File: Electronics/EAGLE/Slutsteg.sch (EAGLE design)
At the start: 151 parts, among them CN1 OSTYK33102030-2, CN2 OSTYK33102030-2, CN3 OSTYK33102030-2, CN4 OSTYK33102030-2, IC1 SPX1117M3-L-3-3_TR, IC10 LM324D, IC11 L78M12ABDT-TR, IC3 ESP32-WROVER-IE-4MB, IC4 TM8211, IC5 LM358LVIDR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

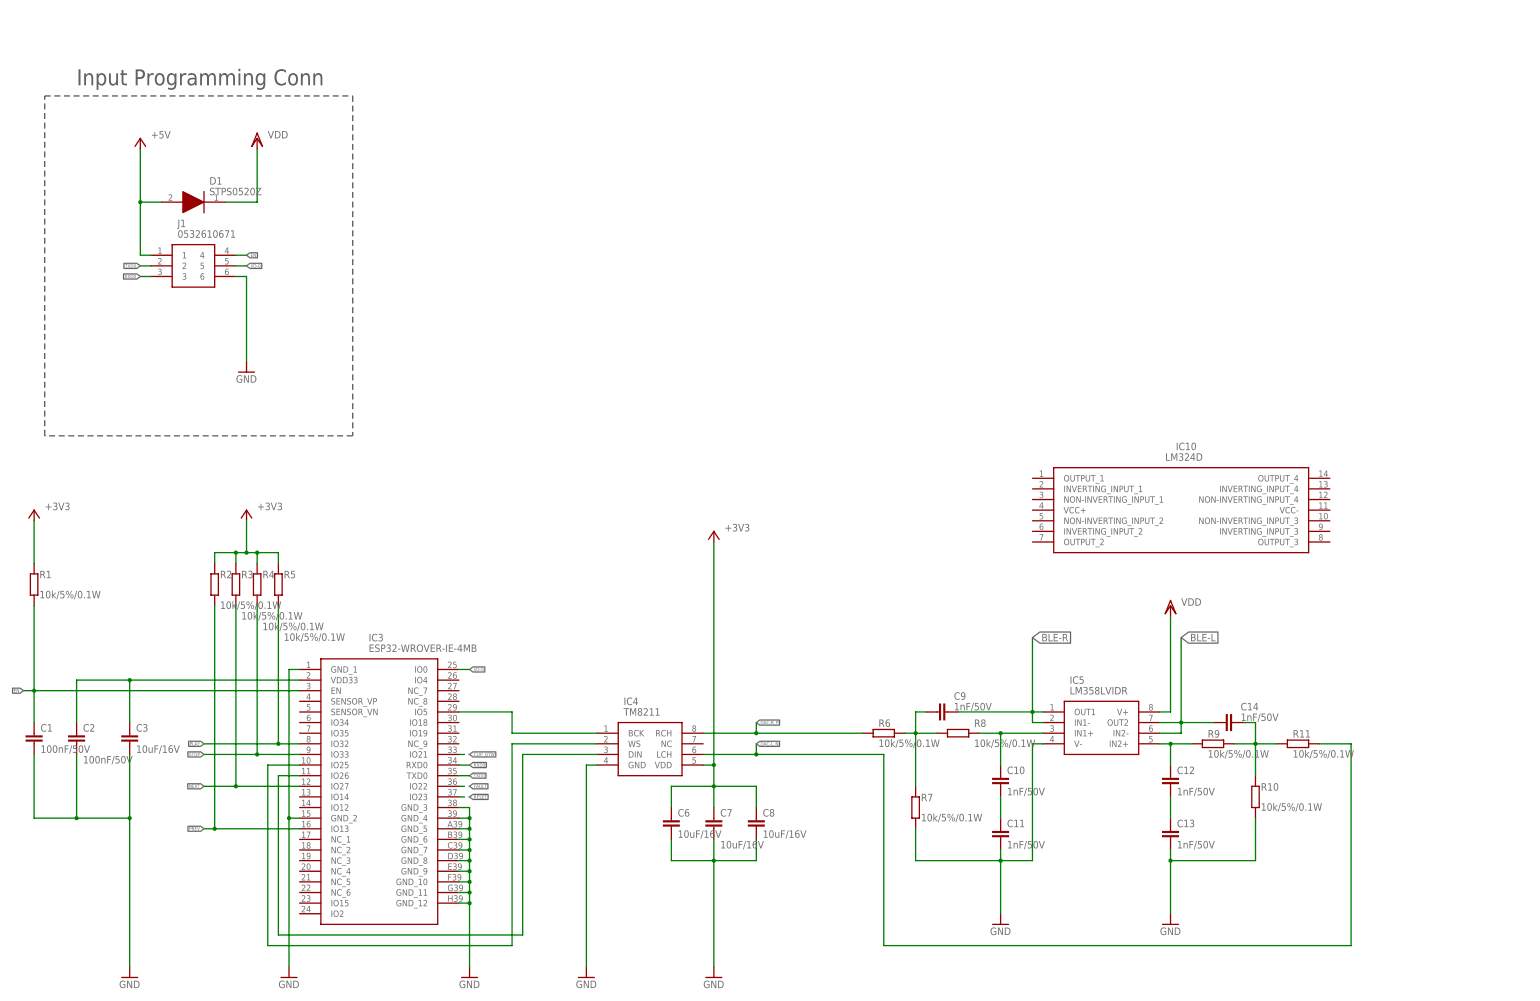
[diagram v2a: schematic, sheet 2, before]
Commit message: Changed OP-AMP for the DAC
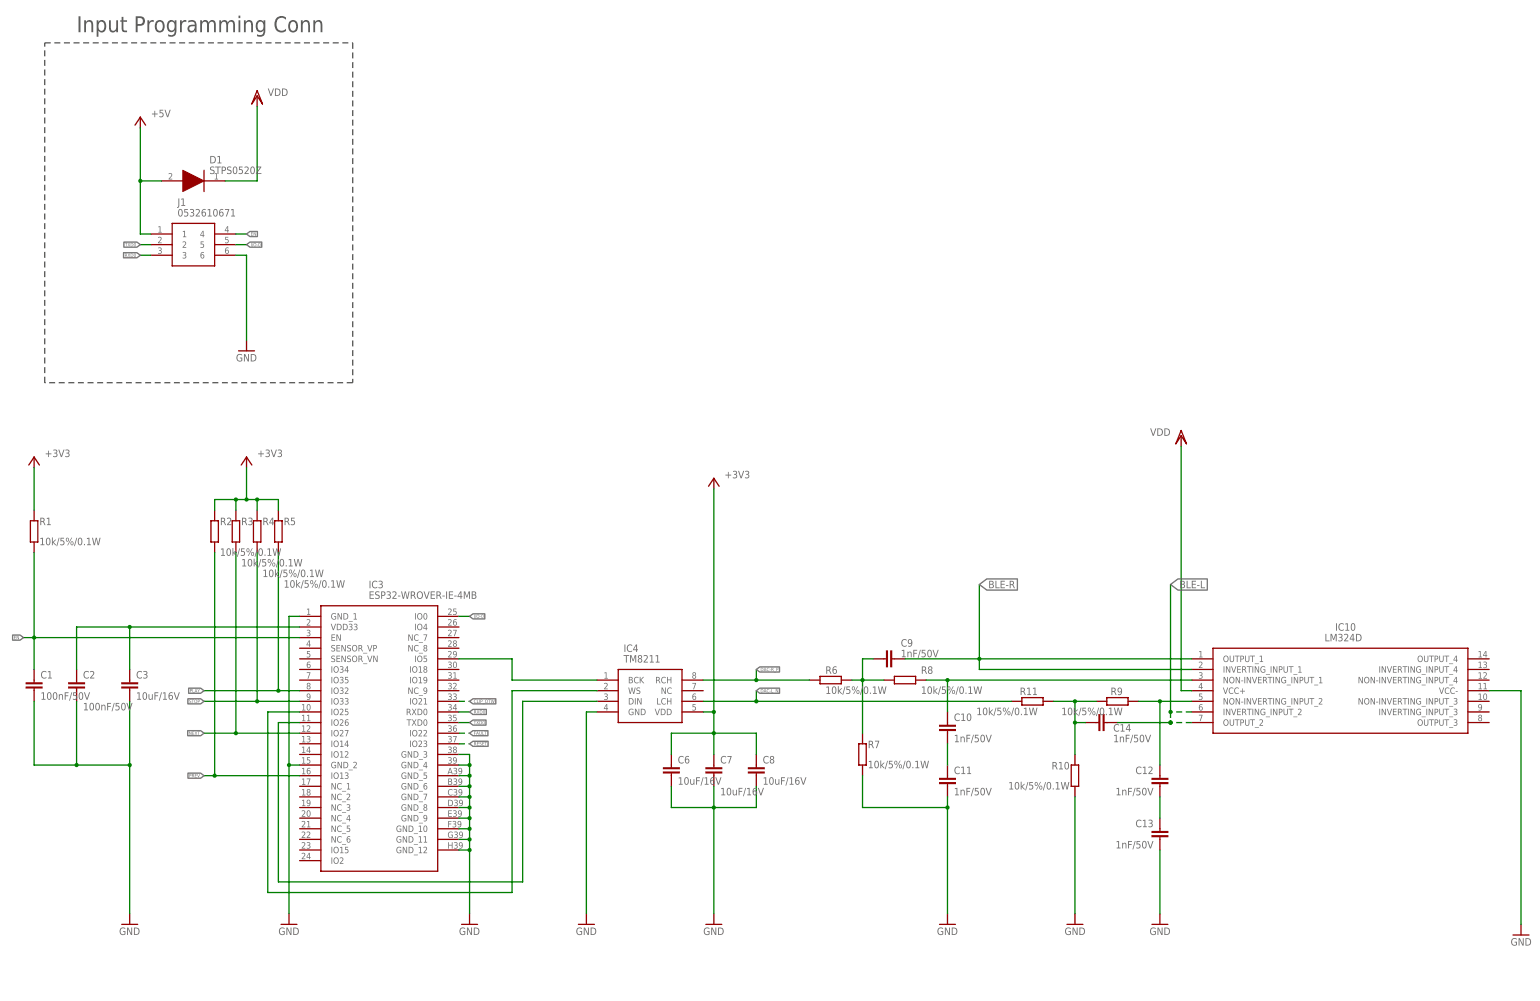
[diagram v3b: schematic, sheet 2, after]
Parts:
- removed IC5: LM358LVIDR, SamacSys_Parts:LM358LVIDR
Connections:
- net BLE-L: now also IC10.INVERTING_INPUT_2, IC10.OUTPUT_2; no longer IC5.IN2-, IC5.OUT2
- net BLE-R: now also IC10.INVERTING_INPUT_1, IC10.OUTPUT_1; no longer IC5.IN1-, IC5.OUT1
- net GND: now also IC10.VCC-; no longer IC5.V-
- net N$79: now also IC10.NON-INVERTING_INPUT_1; no longer IC5.IN1+
- net N$81: now also IC10.NON-INVERTING_INPUT_2; no longer IC5.IN2+
- net VDD: now also IC10.VCC+; no longer IC5.V+
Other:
- moved on the sheet: C1, C10, C11, C12, C13, C14, C2, C3, C5, C6, C7, C8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

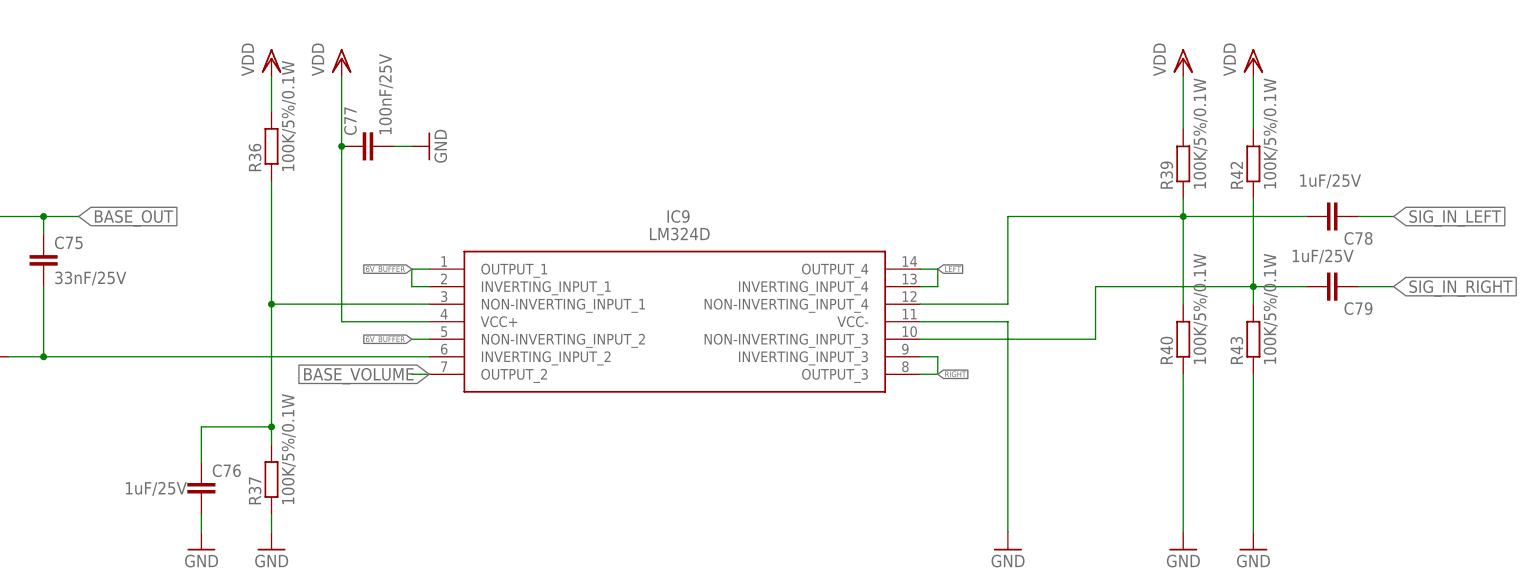
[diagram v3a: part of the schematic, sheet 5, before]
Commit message: Changed footprints for caps
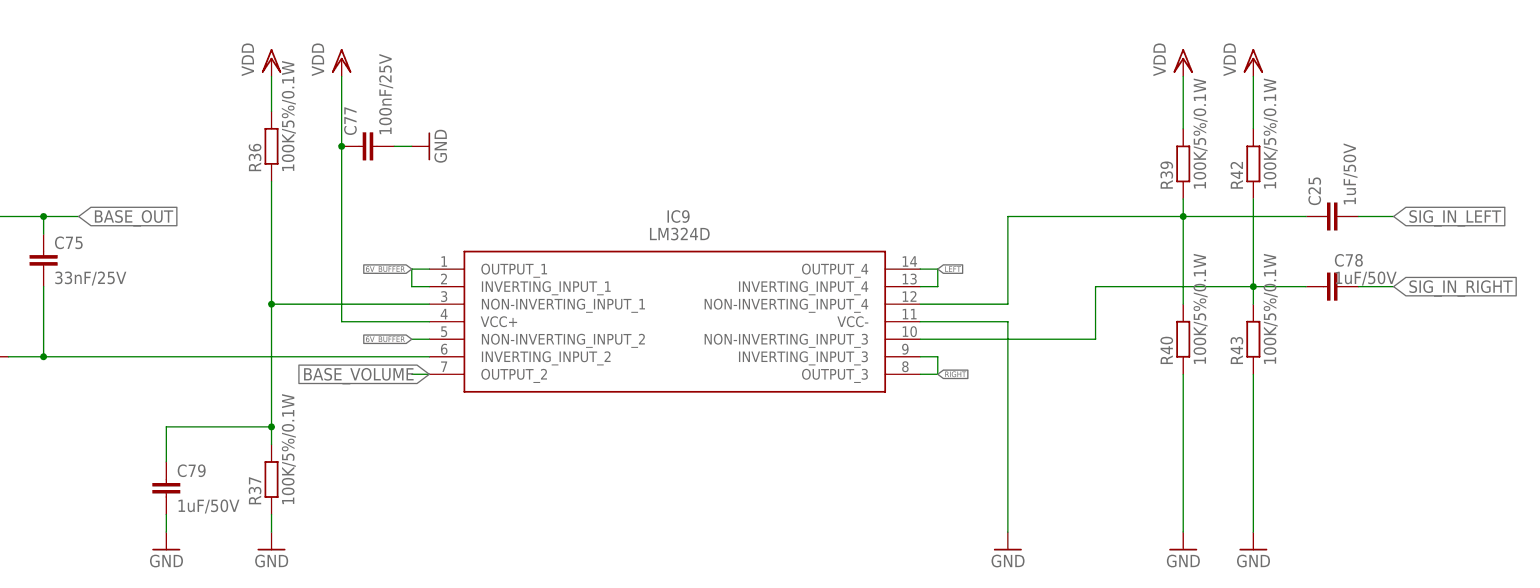
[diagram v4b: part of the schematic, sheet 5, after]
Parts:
- removed C76: 1uF/25V, rcl:C-EUC0603
- added C25: 1uF/50V, rcl:C-EUC0805
- C78, C79: value 1uF/25V -> 1uF/50V; device rcl:C-EUC0603 -> rcl:C-EUC0805
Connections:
- net GND: now also C79.2; no longer C76.2
- net N$46: now also C25.1; no longer C78.2
- net N$47: now also C78.1; no longer C79.2
- net N$50: now also C79.1; no longer C76.1
- net SIG_IN_LEFT: now also C25.2; no longer C78.1
- net SIG_IN_RIGHT: now also C78.2; no longer C79.1
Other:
- moved on the sheet: C78, C79
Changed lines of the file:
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@@
 <part name="R43" library="rcl" library_urn="urn:adsk.eagle:library:334" deviceset="R-EU_" device="R0603" package3d_urn="urn:adsk.eagle:package:23555/3" value="100K/5%/0.1W"/>
 <part name="R42" library="rcl" library_urn="urn:adsk.eagle:library:334" deviceset="R-EU_" device="R0603" package3d_urn="urn:adsk.eagle:package:23555/3" value="100K/5%/0.1W"/>
-<part name="C78" library="rcl" library_urn="urn:adsk.eagle:library:334" deviceset="C-EU" device="C0603" package3d_urn="urn:adsk.eagle:package:23616/2" value="1uF/25V"/>
-<part name="C79" library="rcl" library_urn="urn:adsk.eagle:library:334" deviceset="C-EU" device="C0603" package3d_urn="urn:adsk.eagle:package:23616/2" value="1uF/25V"/>
 <part name="VDD11" library="supply1" library_urn="urn:adsk.eagle:library:371" deviceset="VDD" device=""/>
 <part name="VDD12" library="supply1" library_urn="urn:adsk.eagle:library:371" deviceset="VDD" device=""/>
@@
 <part name="GND37" library="supply1" library_urn="urn:adsk.eagle:library:371" deviceset="GND" device=""/>
 <part name="VDD13" library="supply1" library_urn="urn:adsk.eagle:library:371" deviceset="VDD" device=""/>
-<part name="C76" library="rcl" library_urn="urn:adsk.eagle:library:334" deviceset="C-EU" device="C0603" package3d_urn="urn:adsk.eagle:package:23616/2" value="1uF/25V"/>
 <part name="GND38" library="supply1" library_urn="urn:adsk.eagle:library:371" deviceset="GND" device=""/>
 <part name="R28" library="rcl" library_urn="urn:adsk.eagle:library:334" deviceset="R-EU_" device="R0603" package3d_urn="urn:adsk.eagle:package:23555/3" value="1K/5%/0.1W"/>
@@
 <part name="GND7" library="supply1" library_urn="urn:adsk.eagle:library:371" deviceset="GND" device=""/>
 <part name="GND9" library="supply1" library_urn="urn:adsk.eagle:library:371" deviceset="GND" device=""/>
+<part name="C25" library="rcl" library_urn="urn:adsk.eagle:library:334" deviceset="C-EU" device="C0805" package3d_urn="urn:adsk.eagle:package:23617/2" value="1uF/50V"/>
+<part name="C78" library="rcl" library_urn="urn:adsk.eagle:library:334" deviceset="C-EU" device="C0805" package3d_urn="urn:adsk.eagle:package:23617/2" value="1uF/50V"/>
+<part name="C79" library="rcl" library_urn="urn:adsk.eagle:library:334" deviceset="C-EU" device="C0805" package3d_urn="urn:adsk.eagle:package:23617/2" value="1uF/50V"/>
 </parts>
 <sheets>
@@
 <attribute name="VALUE" x="295.402" y="92.71" size="1.778" layer="96" rot="R90"/>
 </instance>
-<instance part="C78" gate="G$1" x="304.8" y="88.9" smashed="yes" rot="R270">
-<attribute name="NAME" x="305.181" y="84.836" size="1.778" layer="95"/>
-<attribute name="VALUE" x="307.721" y="94.996" size="1.778" layer="96" rot="R180"/>
-</instance>
-<instance part="C79" gate="G$1" x="304.8" y="78.74" smashed="yes" rot="R270">
-<attribute name="NAME" x="305.181" y="74.676" size="1.778" layer="95"/>
-<attribute name="VALUE" x="297.561" y="82.296" size="1.778" layer="96"/>
-</instance>
 <instance part="VDD11" gate="G$1" x="281.94" y="111.76" smashed="yes">
 <attribute name="VALUE" x="279.4" y="109.22" size="1.778" layer="96" rot="R90"/>
@@
 <attribute name="VALUE" x="147.32" y="109.22" size="1.778" layer="96" rot="R90"/>
 </instance>
-<instance part="C76" gate="G$1" x="139.7" y="50.8" smashed="yes">
-<attribute name="NAME" x="141.224" y="51.181" size="1.778" layer="95"/>
-<attribute name="VALUE" x="128.524" y="48.641" size="1.778" layer="96"/>
-</instance>
-<instance part="GND38" gate="1" x="139.7" y="40.64" smashed="yes" rot="MR0">
-<attribute name="VALUE" x="142.24" y="38.1" size="1.778" layer="96" rot="MR0"/>
+<instance part="GND38" gate="1" x="134.62" y="40.64" smashed="yes" rot="MR0">
+<attribute name="VALUE" x="137.16" y="38.1" size="1.778" layer="96" rot="MR0"/>
 </instance>
 <instance part="R28" gate="G$1" x="55.88" y="76.2" smashed="yes" rot="R180">
@@
 <instance part="GND42" gate="1" x="111.76" y="215.9" smashed="yes" rot="MR270">
 <attribute name="VALUE" x="114.3" y="218.44" size="1.778" layer="96" rot="MR270"/>
+</instance>
+<instance part="C25" gate="G$1" x="302.26" y="88.9" smashed="yes" rot="R90">
+<attribute name="NAME" x="301.879" y="90.424" size="1.778" layer="95" rot="R90"/>
+<attribute name="VALUE" x="306.959" y="90.424" size="1.778" layer="96" rot="R90"/>
+</instance>
+<instance part="C78" gate="G$1" x="302.26" y="78.74" smashed="yes" rot="R90">
+<attribute name="NAME" x="303.784" y="81.661" size="1.778" layer="95"/>
+<attribute name="VALUE" x="303.784" y="79.121" size="1.778" layer="96"/>
+</instance>
+<instance part="C79" gate="G$1" x="134.62" y="50.8" smashed="yes">
+<attribute name="NAME" x="136.144" y="51.181" size="1.778" layer="95"/>
+<attribute name="VALUE" x="136.144" y="46.101" size="1.778" layer="96"/>
 </instance>
 </instances>
@@
 </segment>
 <segment>
-<pinref part="C76" gate="G$1" pin="2"/>
 <pinref part="GND38" gate="1" pin="GND"/>
-<wire x1="139.7" y1="45.72" x2="139.7" y2="43.18" width="0.1524" layer="91"/>
+<wire x1="134.62" y1="45.72" x2="134.62" y2="43.18" width="0.1524" layer="91"/>
+<pinref part="C79" gate="G$1" pin="2"/>
 </segment>
 <segment>
@@
 <pinref part="R40" gate="G$1" pin="2"/>
 <wire x1="281.94" y1="91.44" x2="281.94" y2="88.9" width="0.1524" layer="91"/>
-<pinref part="C78" gate="G$1" pin="2"/>
 <wire x1="281.94" y1="88.9" x2="281.94" y2="76.2" width="0.1524" layer="91"/>
 <wire x1="299.72" y1="88.9" x2="281.94" y2="88.9" width="0.1524" layer="91"/>
@@
 <wire x1="256.54" y1="76.2" x2="256.54" y2="88.9" width="0.1524" layer="91"/>
 <wire x1="256.54" y1="88.9" x2="281.94" y2="88.9" width="0.1524" layer="91"/>
+<pinref part="C25" gate="G$1" pin="1"/>
 </segment>
 </net>
@@
 <pinref part="R43" gate="G$1" pin="2"/>
 <wire x1="292.1" y1="91.44" x2="292.1" y2="78.74" width="0.1524" layer="91"/>
-<pinref part="C79" gate="G$1" pin="2"/>
 <wire x1="292.1" y1="78.74" x2="292.1" y2="76.2" width="0.1524" layer="91"/>
 <wire x1="299.72" y1="78.74" x2="292.1" y2="78.74" width="0.1524" layer="91"/>
@@
 <wire x1="269.24" y1="71.12" x2="269.24" y2="78.74" width="0.1524" layer="91"/>
 <wire x1="269.24" y1="78.74" x2="292.1" y2="78.74" width="0.1524" layer="91"/>
+<pinref part="C78" gate="G$1" pin="1"/>
 </segment>
 </net>
 <net name="SIG_IN_RIGHT" class="0">
 <segment>
-<pinref part="C79" gate="G$1" pin="1"/>
 <wire x1="307.34" y1="78.74" x2="312.42" y2="78.74" width="0.1524" layer="91"/>
 <label x="312.42" y="78.74" size="1.778" layer="95" xref="yes"/>
+<pinref part="C78" gate="G$1" pin="2"/>
 </segment>
 </net>
 <net name="SIG_IN_LEFT" class="0">
 <segment>
-<pinref part="C78" gate="G$1" pin="1"/>
 <wire x1="307.34" y1="88.9" x2="312.42" y2="88.9" width="0.1524" layer="91"/>
 <label x="312.42" y="88.9" size="1.778" layer="95" xref="yes"/>
+<pinref part="C25" gate="G$1" pin="2"/>
 </segment>
 </net>
@@
 <pinref part="R37" gate="G$1" pin="2"/>
 <wire x1="149.86" y1="93.98" x2="149.86" y2="76.2" width="0.1524" layer="91"/>
-<pinref part="C76" gate="G$1" pin="1"/>
 <wire x1="149.86" y1="76.2" x2="149.86" y2="58.42" width="0.1524" layer="91"/>
 <wire x1="149.86" y1="58.42" x2="149.86" y2="55.88" width="0.1524" layer="91"/>
-<wire x1="139.7" y1="53.34" x2="139.7" y2="58.42" width="0.1524" layer="91"/>
-<wire x1="139.7" y1="58.42" x2="149.86" y2="58.42" width="0.1524" layer="91"/>
+<wire x1="134.62" y1="53.34" x2="134.62" y2="58.42" width="0.1524" layer="91"/>
+<wire x1="134.62" y1="58.42" x2="149.86" y2="58.42" width="0.1524" layer="91"/>
 <junction x="149.86" y="58.42"/>
 <pinref part="IC9" gate="G$1" pin="NON-INVERTING_INPUT_1"/>
 <wire x1="172.72" y1="76.2" x2="149.86" y2="76.2" width="0.1524" layer="91"/>
 <junction x="149.86" y="76.2"/>
-</segment>
-</net>
+<pinref part="C79" gate="G$1" pin="1"/>
+</segment>
+</net>

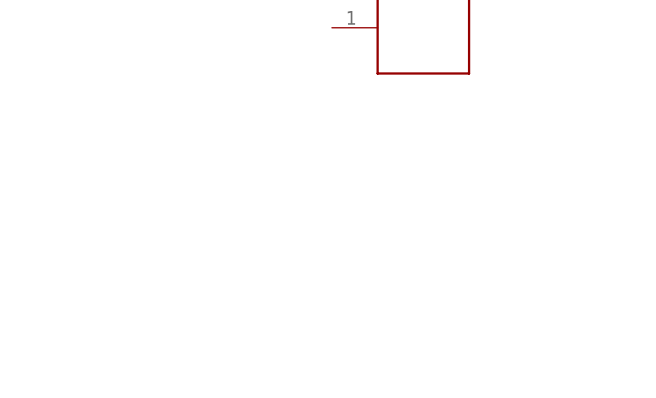
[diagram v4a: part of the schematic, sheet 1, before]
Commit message: Lagt till 3.5mm connector
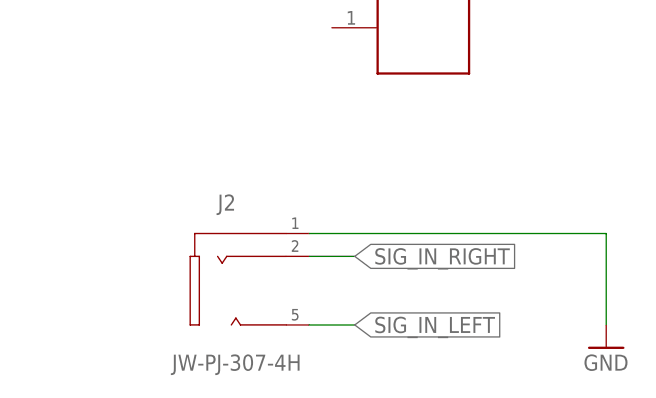
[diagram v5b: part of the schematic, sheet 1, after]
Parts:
- added J2: JW-PJ-307-4H, jack_04:JW-PJ-307-4H
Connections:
- net GND: now also J2.1
- net SIG_IN_LEFT: now also J2.5
- net SIG_IN_RIGHT: now also J2.2
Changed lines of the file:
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@@
 <part name="C78" library="rcl" library_urn="urn:adsk.eagle:library:334" deviceset="C-EU" device="C0805" package3d_urn="urn:adsk.eagle:package:23617/2" value="1uF/50V"/>
 <part name="C79" library="rcl" library_urn="urn:adsk.eagle:library:334" deviceset="C-EU" device="C0805" package3d_urn="urn:adsk.eagle:package:23617/2" value="1uF/50V"/>
+<part name="J2" library="jack_04" deviceset="JW-PJ-307-4" device="H"/>
+<part name="GND10" library="supply1" library_urn="urn:adsk.eagle:library:371" deviceset="GND" device=""/>
 </parts>
 <sheets>
@@
 <attribute name="VALUE" x="99.06" y="154.94" size="1.778" layer="96"/>
 </instance>
+<instance part="J2" gate="G$1" x="327.66" y="99.06" smashed="yes">
+<attribute name="NAME" x="325.12" y="106.68" size="1.778" layer="95"/>
+<attribute name="VALUE" x="320.04" y="88.9" size="1.778" layer="96"/>
+</instance>
+<instance part="GND10" gate="1" x="368.3" y="91.44" smashed="yes">
+<attribute name="VALUE" x="365.76" y="88.9" size="1.778" layer="96"/>
+</instance>
 </instances>
 <busses>
@@
 <wire x1="101.6" y1="160.02" x2="101.6" y2="198.12" width="0.1524" layer="91"/>
 <wire x1="101.6" y1="198.12" x2="111.76" y2="198.12" width="0.1524" layer="91"/>
+</segment>
+<segment>
+<pinref part="GND10" gate="1" pin="GND"/>
+<pinref part="J2" gate="G$1" pin="1"/>
+<wire x1="368.3" y1="93.98" x2="368.3" y2="104.14" width="0.1524" layer="91"/>
+<wire x1="368.3" y1="104.14" x2="335.28" y2="104.14" width="0.1524" layer="91"/>
 </segment>
 </net>
@@
 </segment>
 </net>
+<net name="SIG_IN_RIGHT" class="0">
+<segment>
+<pinref part="J2" gate="G$1" pin="2"/>
+<wire x1="335.28" y1="101.6" x2="340.36" y2="101.6" width="0.1524" layer="91"/>
+<label x="340.36" y="101.6" size="1.778" layer="95" xref="yes"/>
+</segment>
+</net>
+<net name="SIG_IN_LEFT" class="0">
+<segment>
+<pinref part="J2" gate="G$1" pin="5"/>
+<wire x1="335.28" y1="93.98" x2="340.36" y2="93.98" width="0.1524" layer="91"/>
+<label x="340.36" y="93.98" size="1.778" layer="95" xref="yes"/>
+</segment>
+</net>
